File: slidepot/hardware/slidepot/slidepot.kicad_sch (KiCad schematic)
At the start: 3 parts, among them J1 Conn_01x05_Male, J2 Conn_01x02

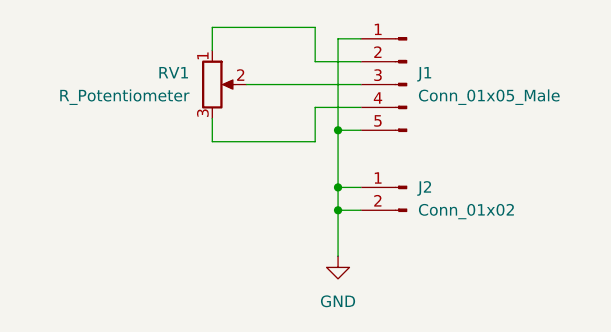
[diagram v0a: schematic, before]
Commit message: Correct direction of input/output connectors for digital signals
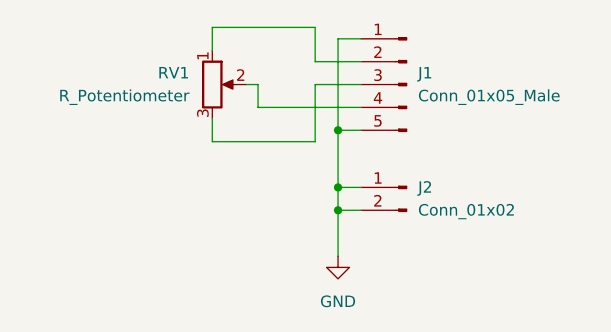
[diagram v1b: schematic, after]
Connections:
- net at J1.3 (Pin_3): now also RV1.3; no longer RV1.2
- net at J1.4 (Pin_4): now also RV1.2; no longer RV1.3
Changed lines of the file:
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@@
   (junction (at 142.24 87.63) (diameter 0) (color 0 0 0 0)
+  )
+  (wire (pts (xy 139.7 76.2) (xy 139.7 82.55))
+    (stroke (width 0) (type default) (color 0 0 0 0))
+  )
+  (wire (pts (xy 144.78 76.2) (xy 139.7 76.2))
+    (stroke (width 0) (type default) (color 0 0 0 0))
   )
   (wire (pts (xy 142.24 87.63) (xy 144.78 87.63))
@@
     (stroke (width 0) (type default) (color 0 0 0 0))
   )
-  (wire (pts (xy 128.27 82.55) (xy 139.7 82.55))
+  (wire (pts (xy 128.27 69.85) (xy 139.7 69.85))
     (stroke (width 0) (type default) (color 0 0 0 0))
   )
-  (wire (pts (xy 132.08 76.2) (xy 144.78 76.2))
+  (wire (pts (xy 133.35 76.2) (xy 133.35 78.74))
     (stroke (width 0) (type default) (color 0 0 0 0))
   )
-  (wire (pts (xy 128.27 69.85) (xy 139.7 69.85))
+  (wire (pts (xy 133.35 78.74) (xy 144.78 78.74))
     (stroke (width 0) (type default) (color 0 0 0 0))
   )
@@
     (stroke (width 0) (type default) (color 0 0 0 0))
   )
+  (wire (pts (xy 132.08 76.2) (xy 133.35 76.2))
+    (stroke (width 0) (type default) (color 0 0 0 0))
+  )
   (wire (pts (xy 142.24 81.28) (xy 144.78 81.28))
     (stroke (width 0) (type default) (color 0 0 0 0))
@@
   )
   (wire (pts (xy 128.27 80.01) (xy 128.27 82.55))
-    (stroke (width 0) (type default) (color 0 0 0 0))
-  )
-  (wire (pts (xy 139.7 82.55) (xy 139.7 78.74))
     (stroke (width 0) (type default) (color 0 0 0 0))
   )
@@
     (stroke (width 0) (type default) (color 0 0 0 0))
   )
-  (wire (pts (xy 139.7 78.74) (xy 144.78 78.74))
+  (wire (pts (xy 139.7 82.55) (xy 128.27 82.55))
     (stroke (width 0) (type default) (color 0 0 0 0))
   )
